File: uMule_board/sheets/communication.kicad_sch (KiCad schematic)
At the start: 1 part, among them J3 ST-LINK

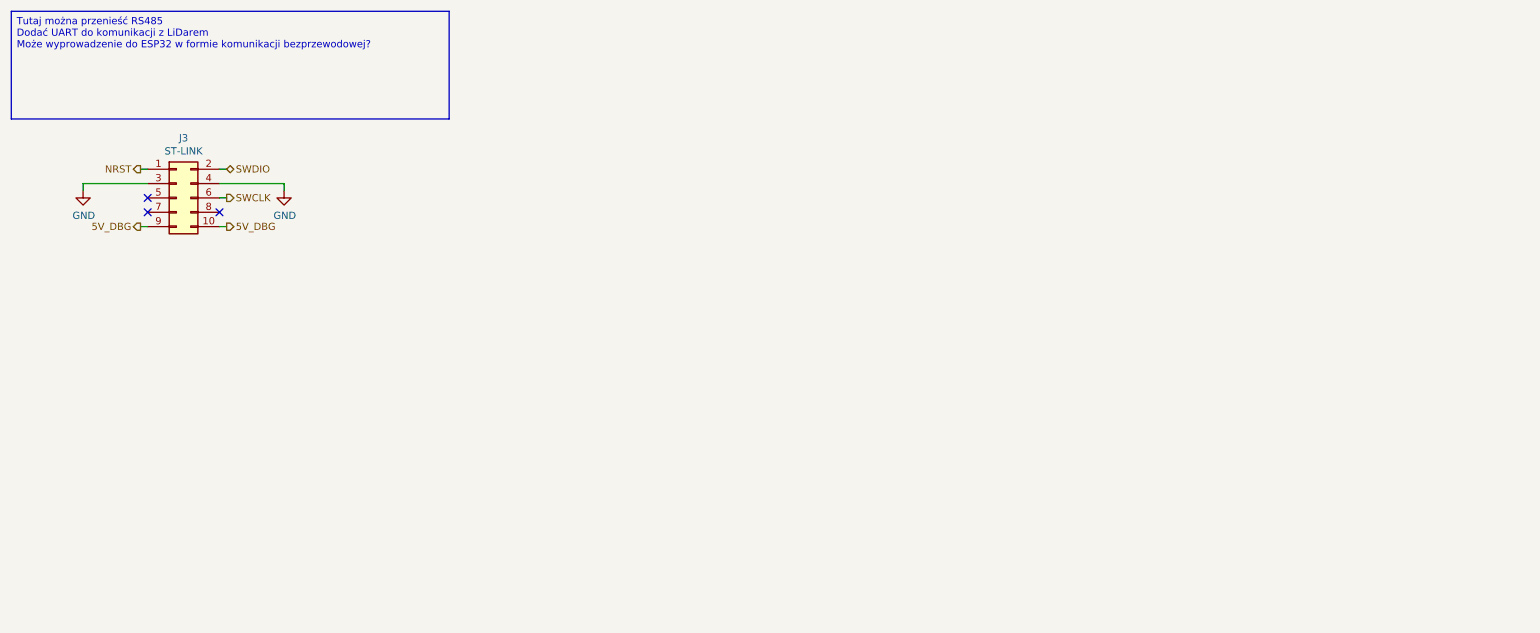
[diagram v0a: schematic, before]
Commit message: Finished schematics. Now ready for PCB
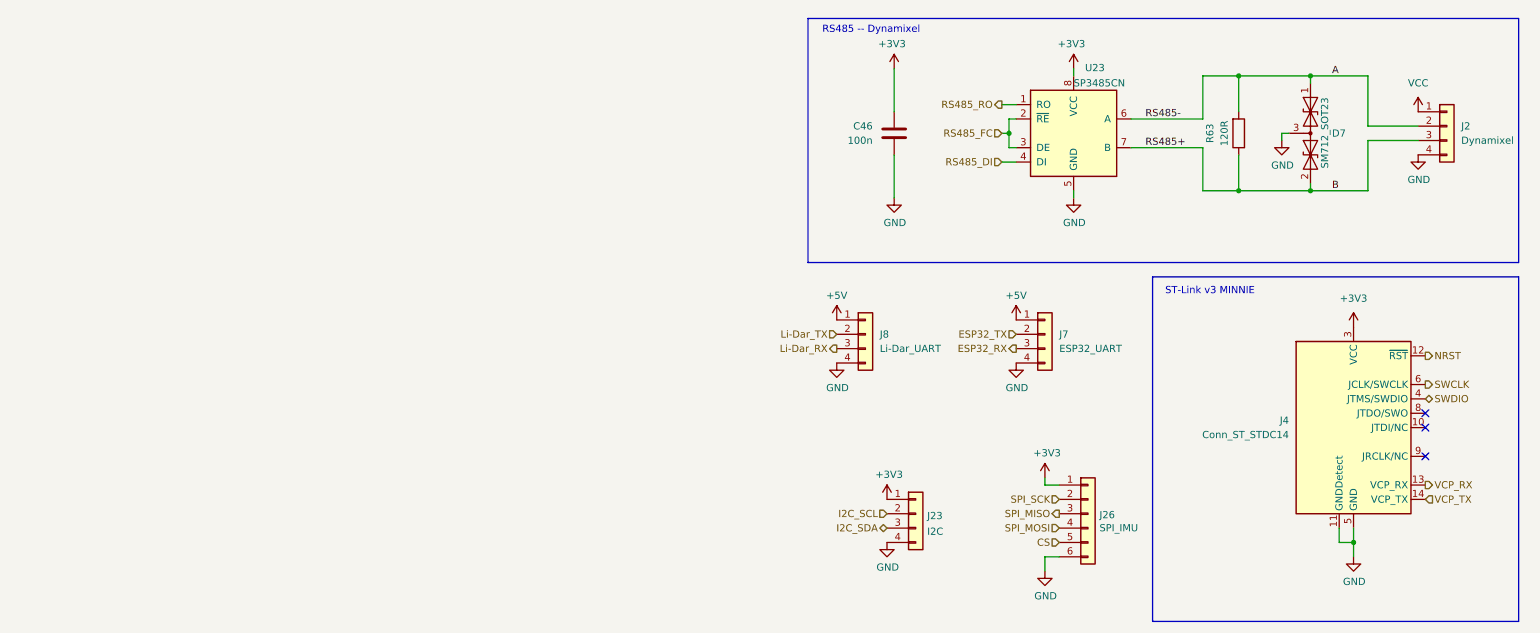
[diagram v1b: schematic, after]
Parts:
- removed J3: ST-LINK, Connector_IDC:IDC-Header_2x05_P2.54mm_Vertical, symbol Connector_Generic:Conn_02x05_Odd_Even
- added C46: 100n, Capacitor_SMD:C_0603_1608Metric, symbol Device:C
- added D7: SM712_SOT23, Package_TO_SOT_SMD:SOT-23, symbol Diode:SM712_SOT23
- added J2: Dynamixel, Connector_JST:JST_XH_B4B-XH-A_1x04_P2.50mm_Vertical, symbol Connector_Generic:Conn_01x04
- added J23: I2C, Connector_JST:JST_XH_B4B-XH-A_1x04_P2.50mm_Vertical, symbol Connector_Generic:Conn_01x04
- added J26: SPI_IMU, Connector_JST:JST_XH_B6B-XH-A_1x06_P2.50mm_Vertical, symbol Connector_Generic:Conn_01x06
- added J4: Conn_ST_STDC14, Connector_PinHeader_1.27mm:PinHeader_2x07_P1.27mm_Vertical, symbol Connector:Conn_ST_STDC14
- added J7: ESP32_UART, Connector_JST:JST_XH_B4B-XH-A_1x04_P2.50mm_Vertical, symbol Connector_Generic:Conn_01x04
- added J8: Li-Dar_UART, Connector_JST:JST_XH_B4B-XH-A_1x04_P2.50mm_Vertical, symbol Connector_Generic:Conn_01x04
- added R63: 120R, Resistor_SMD:R_0603_1608Metric, symbol Device:R
- added U23: SP3485CN, Package_SO:SOIC-8_3.9x4.9mm_P1.27mm, symbol Interface_UART:SP3485CN
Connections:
- net GND: now also C46.1, D7.3 (common), J2.4 (Pin_4), J23.4 (Pin_4), J26.6 (Pin_6), J4.11 (GNDDetect), J4.5 (GND), J4.7 (GND), J7.4 (Pin_4), J8.4 (Pin_4), U23.5 (GND)
- net NRST: now also J4.12 (~{RST})
- net SWCLK: now also J4.6 (JCLK/SWCLK)
- net SWDIO: now also J4.4 (JTMS/SWDIO)
- new net +3V3: C46.2, J23.1 (Pin_1), J26.1 (Pin_1), J4.3 (VCC), U23.8 (VCC)
- new net +5V: J7.1 (Pin_1), J8.1 (Pin_1)
- new net A: D7.1 (A1), J2.2 (Pin_2), R63.2, U23.6 (A)
- new net B: D7.2 (A2), J2.3 (Pin_3), R63.1, U23.7 (B)
- new net CS: J26.5 (Pin_5)
- new net ESP32_RX: J7.3 (Pin_3)
- new net ESP32_TX: J7.2 (Pin_2)
- new net I2C_SCL: J23.2 (Pin_2)
- new net I2C_SDA: J23.3 (Pin_3)
- new net Li-Dar_RX: J8.3 (Pin_3)
- new net Li-Dar_TX: J8.2 (Pin_2)
- new net RS485_DI: U23.4 (DI)
- new net RS485_FC: U23.2 (~{RE}), U23.3 (DE)
- new net RS485_RO: U23.1 (RO)
- new net SPI_MISO: J26.3 (Pin_3)
- new net SPI_MOSI: J26.4 (Pin_4)
- new net SPI_SCK: J26.2 (Pin_2)
- new net VCC: J2.1 (Pin_1)
- new net VCP_RX: J4.13 (VCP_RX)
- new net VCP_TX: J4.14 (VCP_TX)
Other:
- note added: "RS485 -- Dynamixel"
- note added: "ST-Link v3 MINNIE"

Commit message: Started working on PCB. Ditched high power outputs. Focusing on photodiodes. One commit closer to order
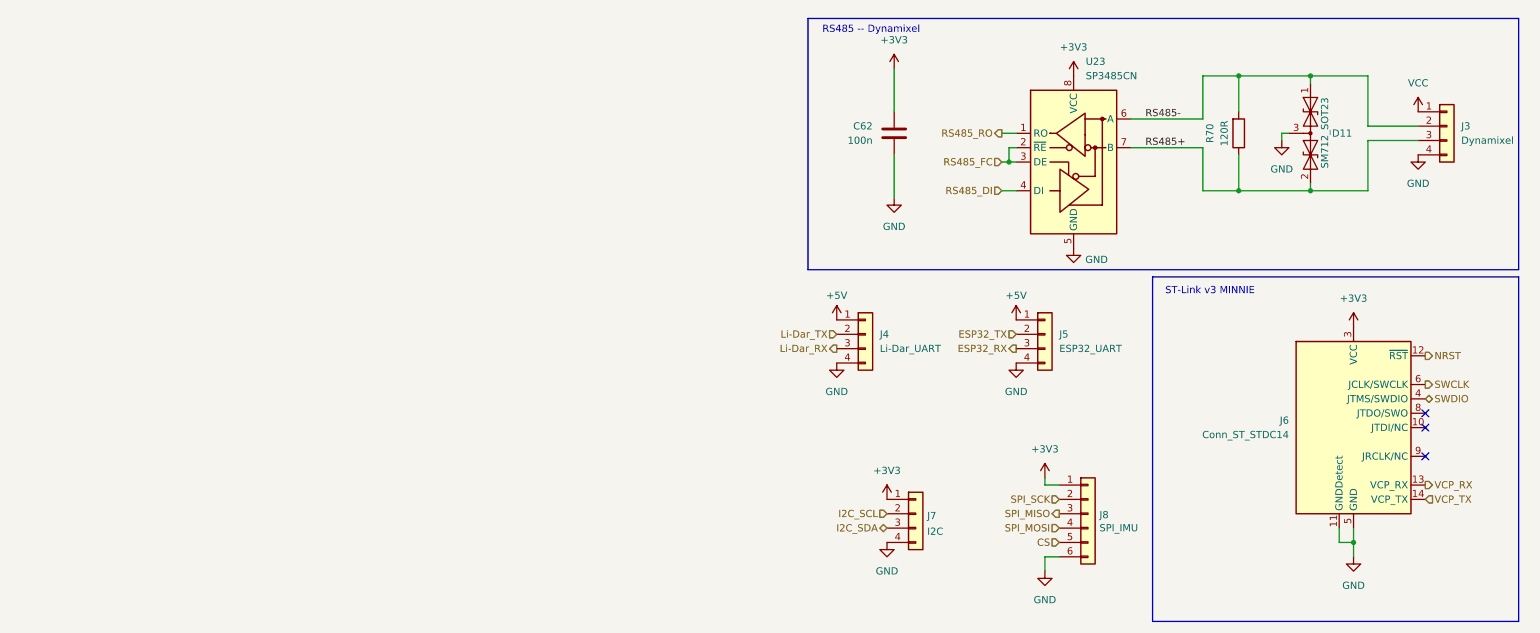
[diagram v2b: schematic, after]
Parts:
- renumbered C46 to C62, D7 to D11, J2 to J3, J8 to J4, J7 to J5, J4 to J6, J23 to J7, J26 to J8, R63 to R70
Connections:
- net A renamed RS485-
- net B renamed RS485+
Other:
- title: (none) -> uMule_board

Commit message: sch ready, only missing the pcb
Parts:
- renumbered C62 to C50, J3 to J2, J4 to J3, J5 to J4, J6 to J5, J7 to J6, J8 to J7, R70 to R37, U23 to U16
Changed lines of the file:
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@@
 		(on_board yes)
 		(dnp no)
-		(property "Reference" "R70"
+		(property "Reference" "R37"
 			(at 227.33 35.56 90)
 			(effects
@@
 			(project "uMule_board"
 				(path "/3d853824-a92e-40a5-ad1a-5052c8a0bd68/09940b78-7107-436f-9fae-587995b124f4"
-					(reference "R70")
+					(reference "R37")
 					(unit 1)
 				)
@@
 		(on_board yes)
 		(dnp no)
-		(property "Reference" "#PWR0117"
+		(property "Reference" "#PWR081"
 			(at 161.29 72.39 0)
 			(effects
@@
 			(project "uMule_board"
 				(path "/3d853824-a92e-40a5-ad1a-5052c8a0bd68/09940b78-7107-436f-9fae-587995b124f4"
-					(reference "#PWR0117")
+					(reference "#PWR081")
 					(unit 1)
 				)
@@
 		(dnp no)
 		(fields_autoplaced yes)
-		(property "Reference" "#PWR0113"
+		(property "Reference" "#PWR077"
 			(at 240.03 43.18 0)
 			(effects
@@
 			(project "uMule_board"
 				(path "/3d853824-a92e-40a5-ad1a-5052c8a0bd68/09940b78-7107-436f-9fae-587995b124f4"
-					(reference "#PWR0113")
+					(reference "#PWR077")
 					(unit 1)
 				)
@@
 		(dnp no)
 		(fields_autoplaced yes)
-		(property "Reference" "J3"
+		(property "Reference" "J2"
 			(at 271.78 34.2899 0)
 			(effects
@@
 			(project "uMule_board"
 				(path "/3d853824-a92e-40a5-ad1a-5052c8a0bd68/09940b78-7107-436f-9fae-587995b124f4"
-					(reference "J3")
+					(reference "J2")
 					(unit 1)
 				)
@@
 		(on_board yes)
 		(dnp no)
-		(property "Reference" "#PWR0116"
+		(property "Reference" "#PWR080"
 			(at 203.2 62.23 0)
 			(effects
@@
 			(project "uMule_board"
 				(path "/3d853824-a92e-40a5-ad1a-5052c8a0bd68/09940b78-7107-436f-9fae-587995b124f4"
-					(reference "#PWR0116")
+					(reference "#PWR080")
 					(unit 1)
 				)
@@
 		(dnp no)
 		(fields_autoplaced yes)
-		(property "Reference" "J6"
+		(property "Reference" "J5"
 			(at 241.3 86.3599 0)
 			(effects
@@
 			(project ""
 				(path "/3d853824-a92e-40a5-ad1a-5052c8a0bd68/09940b78-7107-436f-9fae-587995b124f4"
-					(reference "J6")
+					(reference "J5")
 					(unit 1)
 				)
@@
 		(dnp no)
 		(fields_autoplaced yes)
-		(property "Reference" "#PWR0112"
+		(property "Reference" "#PWR076"
 			(at 264.16 35.56 0)
 			(effects
@@
 			(project "uMule_board"
 				(path "/3d853824-a92e-40a5-ad1a-5052c8a0bd68/09940b78-7107-436f-9fae-587995b124f4"
-					(reference "#PWR0112")
+					(reference "#PWR076")
 					(unit 1)
 				)
@@
 		(dnp no)
 		(fields_autoplaced yes)
-		(property "Reference" "#PWR0119"
+		(property "Reference" "#PWR083"
 			(at 252.73 73.66 0)
 			(effects
@@
 			(project ""
 				(path "/3d853824-a92e-40a5-ad1a-5052c8a0bd68/09940b78-7107-436f-9fae-587995b124f4"
-					(reference "#PWR0119")
+					(reference "#PWR083")
 					(unit 1)
 				)
@@
 		(dnp no)
 		(fields_autoplaced yes)
-		(property "Reference" "U23"
+		(property "Reference" "U16"
 			(at 205.3433 22.86 0)
 			(effects
@@
 			(project ""
 				(path "/3d853824-a92e-40a5-ad1a-5052c8a0bd68/09940b78-7107-436f-9fae-587995b124f4"
-					(reference "U23")
+					(reference "U16")
 					(unit 1)
 				)
@@
 		(dnp no)
 		(fields_autoplaced yes)
-		(property "Reference" "J4"
+		(property "Reference" "J3"
 			(at 168.91 71.1199 0)
 			(effects
@@
 			(project "uMule_board"
 				(path "/3d853824-a92e-40a5-ad1a-5052c8a0bd68/09940b78-7107-436f-9fae-587995b124f4"
-					(reference "J4")
+					(reference "J3")
 					(unit 1)
 				)
@@
 		(on_board yes)
 		(dnp no)
-		(property "Reference" "J8"
+		(property "Reference" "J7"
 			(at 207.772 103.0732 0)
 			(effects
@@
 			(project "uMule_board"
 				(path "/3d853824-a92e-40a5-ad1a-5052c8a0bd68/09940b78-7107-436f-9fae-587995b124f4"
-					(reference "J8")
+					(reference "J7")
 					(unit 1)
 				)
@@
 		(dnp no)
 		(fields_autoplaced yes)
-		(property "Reference" "#PWR0122"
+		(property "Reference" "#PWR086"
 			(at 198.12 100.33 0)
 			(effects
@@
 			(project "uMule_board"
 				(path "/3d853824-a92e-40a5-ad1a-5052c8a0bd68/09940b78-7107-436f-9fae-587995b124f4"
-					(reference "#PWR0122")
+					(reference "#PWR086")
 					(unit 1)
 				)
@@
 		(dnp no)
 		(fields_autoplaced yes)
-		(property "Reference" "#PWR0126"
+		(property "Reference" "#PWR090"
 			(at 198.12 119.38 0)
 			(effects
@@
 			(project "uMule_board"
 				(path "/3d853824-a92e-40a5-ad1a-5052c8a0bd68/09940b78-7107-436f-9fae-587995b124f4"
-					(reference "#PWR0126")
+					(reference "#PWR090")
 					(unit 1)
 				)
@@
 		(dnp no)
 		(fields_autoplaced yes)
-		(property "Reference" "#PWR0120"
+		(property "Reference" "#PWR084"
 			(at 161.29 82.55 0)
 			(effects
@@
 			(project "uMule_board"
 				(path "/3d853824-a92e-40a5-ad1a-5052c8a0bd68/09940b78-7107-436f-9fae-587995b124f4"
-					(reference "#PWR0120")
+					(reference "#PWR084")
 					(unit 1)
 				)
@@
 		(dnp no)
 		(fields_autoplaced yes)
-		(property "Reference" "J5"
+		(property "Reference" "J4"
 			(at 200.66 71.1199 0)
 			(effects
@@
 			(project "uMule_board"
 				(path "/3d853824-a92e-40a5-ad1a-5052c8a0bd68/09940b78-7107-436f-9fae-587995b124f4"
-					(reference "J5")
+					(reference "J4")
 					(unit 1)
 				)
@@
 		(dnp no)
 		(fields_autoplaced yes)
-		(property "Reference" "#PWR0123"
+		(property "Reference" "#PWR087"
 			(at 170.18 104.14 0)
 			(effects
@@
 			(project "uMule_board"
 				(path "/3d853824-a92e-40a5-ad1a-5052c8a0bd68/09940b78-7107-436f-9fae-587995b124f4"
-					(reference "#PWR0123")
+					(reference "#PWR087")
 					(unit 1)
 				)
@@
 		(dnp no)
 		(fields_autoplaced yes)
-		(property "Reference" "J7"
+		(property "Reference" "J6"
 			(at 177.292 103.2315 0)
 			(effects
@@
 			(project "uMule_board"
 				(path "/3d853824-a92e-40a5-ad1a-5052c8a0bd68/09940b78-7107-436f-9fae-587995b124f4"
-					(reference "J7")
+					(reference "J6")
 					(unit 1)
 				)
@@
 		(dnp no)
 		(fields_autoplaced yes)
-		(property "Reference" "#PWR0121"
+		(property "Reference" "#PWR085"
 			(at 193.04 82.55 0)
 			(effects
@@
 			(project "uMule_board"
 				(path "/3d853824-a92e-40a5-ad1a-5052c8a0bd68/09940b78-7107-436f-9fae-587995b124f4"
-					(reference "#PWR0121")
+					(reference "#PWR085")
 					(unit 1)
 				)
@@
 		(dnp no)
 		(fields_autoplaced yes)
-		(property "Reference" "#PWR0124"
+		(property "Reference" "#PWR088"
 			(at 170.18 114.3 0)
 			(effects
@@
 			(project "uMule_board"
 				(path "/3d853824-a92e-40a5-ad1a-5052c8a0bd68/09940b78-7107-436f-9fae-587995b124f4"
-					(reference "#PWR0124")
+					(reference "#PWR088")
 					(unit 1)
 				)
@@
 		(dnp no)
 		(fields_autoplaced yes)
-		(property "Reference" "#PWR0114"
+		(property "Reference" "#PWR078"
 			(at 264.16 45.72 0)
 			(effects
@@
 			(project "uMule_board"
 				(path "/3d853824-a92e-40a5-ad1a-5052c8a0bd68/09940b78-7107-436f-9fae-587995b124f4"
-					(reference "#PWR0114")
+					(reference "#PWR078")
 					(unit 1)
 				)
@@
 		(dnp no)
 		(fields_autoplaced yes)
-		(property "Reference" "#PWR0110"
+		(property "Reference" "#PWR074"
 			(at 171.45 27.94 0)
 			(effects
@@
 			(project "uMule_board"
 				(path "/3d853824-a92e-40a5-ad1a-5052c8a0bd68/09940b78-7107-436f-9fae-587995b124f4"
-					(reference "#PWR0110")
+					(reference "#PWR074")
 					(unit 1)
 				)
@@
 		(dnp no)
 		(fields_autoplaced yes)
-		(property "Reference" "C62"
+		(property "Reference" "C50"
 			(at 167.64 34.2899 0)
 			(effects
@@
 			(project "uMule_board"
 				(path "/3d853824-a92e-40a5-ad1a-5052c8a0bd68/09940b78-7107-436f-9fae-587995b124f4"
-					(reference "C62")
+					(reference "C50")
 					(unit 1)
 				)
@@
 		(dnp no)
 		(fields_autoplaced yes)
-		(property "Reference" "#PWR0115"
+		(property "Reference" "#PWR079"
 			(at 171.45 53.34 0)
 			(effects
@@
 			(project ""
 				(path "/3d853824-a92e-40a5-ad1a-5052c8a0bd68/09940b78-7107-436f-9fae-587995b124f4"
-					(reference "#PWR0115")
+					(reference "#PWR079")
 					(unit 1)
 				)
@@
 		(on_board yes)
 		(dnp no)
-		(property "Reference" "#PWR0118"
+		(property "Reference" "#PWR082"
 			(at 193.04 72.39 0)
 			(effects
@@
 			(project "uMule_board"
 				(path "/3d853824-a92e-40a5-ad1a-5052c8a0bd68/09940b78-7107-436f-9fae-587995b124f4"
-					(reference "#PWR0118")
+					(reference "#PWR082")
 					(unit 1)
 				)
@@
 		(dnp no)
 		(fields_autoplaced yes)
-		(property "Reference" "#PWR0111"
+		(property "Reference" "#PWR075"
 			(at 203.2 29.21 0)
 			(effects
@@
 			(project "uMule_board"
 				(path "/3d853824-a92e-40a5-ad1a-5052c8a0bd68/09940b78-7107-436f-9fae-587995b124f4"
-					(reference "#PWR0111")
+					(reference "#PWR075")
 					(unit 1)
 				)
@@
 		(dnp no)
 		(fields_autoplaced yes)
-		(property "Reference" "#PWR0125"
+		(property "Reference" "#PWR089"
 			(at 252.73 116.84 0)
 			(effects
@@
 			(project "uMule_board"
 				(path "/3d853824-a92e-40a5-ad1a-5052c8a0bd68/09940b78-7107-436f-9fae-587995b124f4"
-					(reference "#PWR0125")
-					(unit 1)
-				)
+					(reference "#PWR089")
+					(unit 1)
+				)
